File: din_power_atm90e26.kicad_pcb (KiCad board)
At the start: 2 copper layers, 86.9 x 32.8 mm, 62 parts, among them J1 CONN_01X06, J2 VBAT, J3 CONN_01X08, J4 CONN_02X18, J5 CONN_01X08, U1 MCP73831-2-OT, U2 AP7365-33YG-13, U3 AP7365-33YG-13, U4 Hi-Link_SMPS, U5 dc-dc

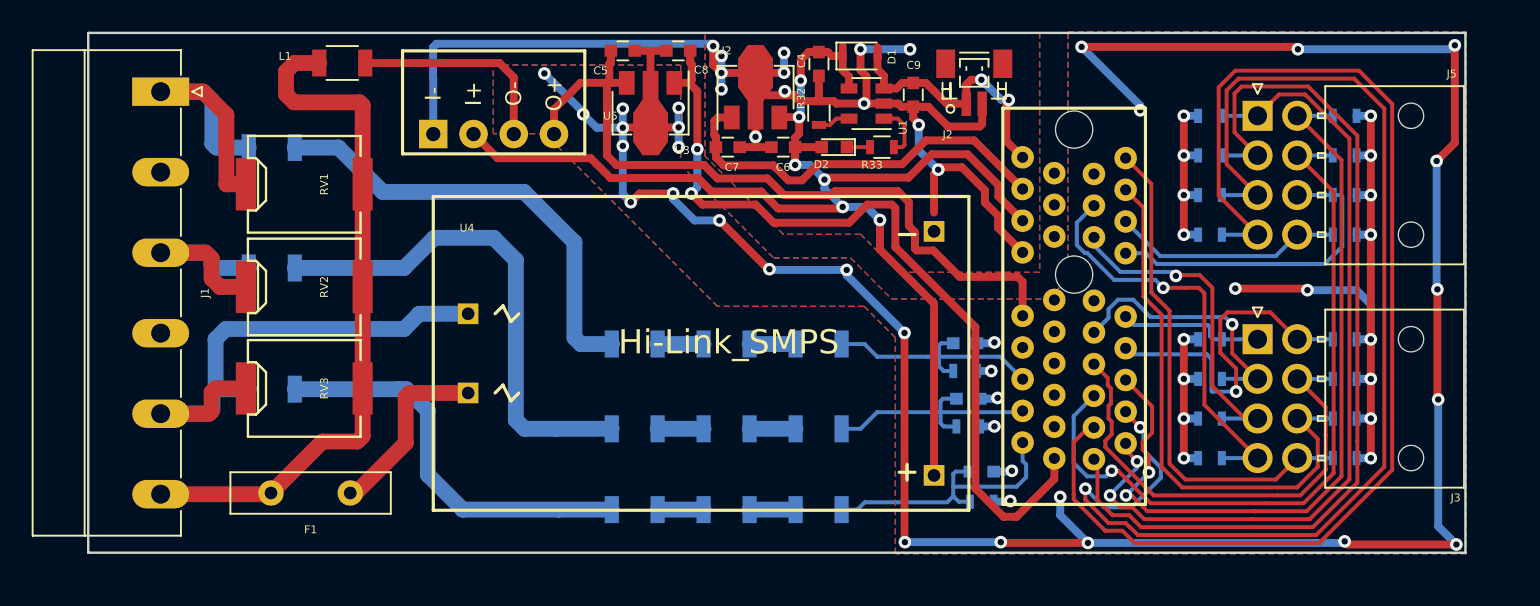
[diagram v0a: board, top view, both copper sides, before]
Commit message: First pass at layout matching meter PCB
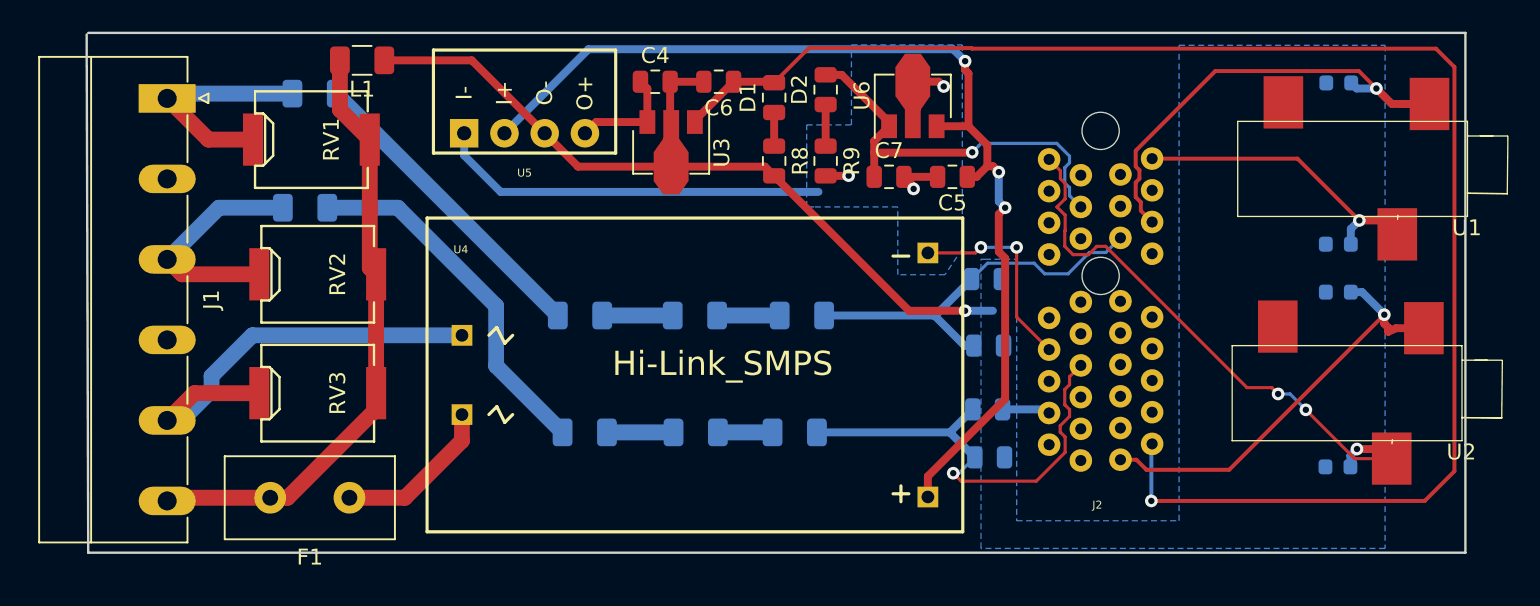
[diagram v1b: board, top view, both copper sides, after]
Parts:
- removed C2: 33n, Capacitors_SMD:C_0603
- removed C8, C9: 1uF, Capacitors_SMD:C_0603
- removed J3, J5: CONN_01X08, Connectors_Molex:Molex_NanoFit_2x04x2.50mm_Angled
- removed J4: CONN_02X18, hi-link_smps:PCIE-36-SKT
- removed LOGO_OSHW1: Logo_Open_Hardware_Small, Symbols:OSHW-Symbol_6.7x6mm_SilkScreen
- removed R10, R11, R18, R19, R20, R21, R28, R29, R30, R31: 5.8R, Resistors_SMD:R_0603
- removed R14, R17, R24, R7: 220K, Resistors_SMD:R_1206
- removed R27, R33: 1K, Resistors_SMD:R_0603
- removed R32: 2K, Resistors_SMD:R_0603
- added U6: AP7365-33YG-13, Package_TO_SOT_SMD:SOT-89-3, F.Cu at (157.9, 49.9)
- C1, C3: value 33n -> .033u; footprint Capacitors_SMD:C_0603 -> Capacitor_SMD:C_0805_2012Metric
- C4, C5, C6, C7: value 1uF -> 1u; footprint Capacitors_SMD:C_0603 -> Capacitor_SMD:C_0805_2012Metric
- D1: value D_Schottky -> IND_LED; footprint Diodes_SMD:D_SOD-323F -> Capacitor_SMD:C_0805_2012Metric
- D2: value LED -> IND_LED; footprint LEDs:LED_0603 -> Capacitor_SMD:C_0805_2012Metric
- F1: footprint Capacitors_THT:C_Disc_D10.0mm_W2.5mm_P5.00mm -> Capacitor_THT:C_Disc_D10.5mm_W5.0mm_P5.00mm
- J2: value VBAT -> CONN_02X18; footprint Connectors_JST:JST_SH_BM02B-SRSS-TB_02x1.00mm_Straight -> hi-link_smps:PCIE-36-SKT
- L1: footprint Inductors_SMD:L_1206 -> Inductor_SMD:L_1206_3216Metric
- R1, R2, R3, R4: footprint Resistors_SMD:R_0603 -> Resistor_SMD:R_0603_1608Metric
- R12, R13, R15, R16, R22, R23, R5, R6: footprint Resistors_SMD:R_1206 -> Resistor_SMD:R_1206_3216Metric
- R25, R26: footprint Resistors_SMD:R_0603 -> Resistor_SMD:R_0805_2012Metric
- R8, R9: value 5.8R -> 499; footprint Resistors_SMD:R_0603 -> Resistor_SMD:R_0805_2012Metric; moved to F.Cu
- U1: value MCP73831-2-OT -> TRS35_3; footprint TO_SOT_Packages_SMD:SOT-23-5 -> HappyDayEnergyMonitor:Audio-Jack
- U2: value AP7365-33YG-13 -> TRS35_3; footprint TO_SOT_Packages_SMD:SOT-89-3 -> HappyDayEnergyMonitor:Audio-Jack
- U3: footprint TO_SOT_Packages_SMD:SOT-89-3 -> Package_TO_SOT_SMD:SOT-89-3
- moved U2 49.7 mm to (192.6, 71.2), turned to 180 degrees
- moved U1 38.6 mm to (192.9, 57.0)
- moved R8 27.6 mm to (149.2, 53.5), turned to 270 degrees
- moved R9 24.7 mm to (152.4, 53.5), turned to 270 degrees
- moved C5 22.3 mm to (160.4, 54.5), turned to 180 degrees
- moved R4 19.7 mm to (184.8, 72.8), turned to 180 degrees
- moved SYM1 16.0 mm to (132.3, 57.9)
- moved J2 14.5 mm to (169.8, 60.8), turned to 90 degrees
- moved R3 11.1 mm to (184.8, 61.8), turned to 0 degrees
- moved C4 10.4 mm to (141.7, 48.5), turned to 0 degrees
- moved C7 10.3 mm to (156.4, 54.5)
- moved R2 9.85 mm to (184.8, 58.8)
- moved R1 8.39 mm to (184.8, 48.6)
- moved D1 6.03 mm to (149.2, 49.5), turned to 90 degrees
- moved C6 5.80 mm to (145.7, 48.5)
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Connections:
- C1 pad 1: UB_SAMP -> VP_1
- C1 pad 2: GNDA -> GND_M
- C3 pad 1: UA_SAMP -> VP_0
- C3 pad 2: GNDA -> GND_M
- C4 pad 1: +5V -> +5V_ISO
- C4 pad 2: GNDPWR -> GND_M
- C5 pad 1: +5V_ISO -> +5V
- C5 pad 2: GNDA -> GND_CPU
- C6 pad 1: +5V -> 3V3_M
- C6 pad 2: GNDPWR -> GND_M
- C7 pad 1: +3V3 -> 3V3_CPU
- C7 pad 2: GNDPWR -> GND_CPU
- D1 pad 1: +5V -> Net-(D1-Pad1)
- D1 pad 2: VBAT -> 3V3_M
- D2 pad 2: +5V -> 3V3_CPU
- J2 pad 1: VBAT -> 3V3_M
- J2 pad 2: GNDPWR -> VP_1
- L1 pad 1: GNDA -> GND_M
- R1 pad 1: GNDA -> GND_M
- R1 pad 2: IA1+ -> I1P_0_IN
- R2 pad 1: IA1- -> I1N_0_N
- R2 pad 2: GNDA -> GND_M
- R22 pad 1: UA_SAMP -> VP_0
- R23 pad 1: UB_SAMP -> VP_1
- R25 pad 1: GNDA -> GND_M
- R25 pad 2: UA_SAMP -> VP_0
- R26 pad 1: GNDA -> GND_M
- R26 pad 2: UB_SAMP -> VP_1
- R3 pad 1: GNDA -> GND_M
- R3 pad 2: IC1+ -> I1P_1_IN
- R4 pad 1: IC1- -> I1N_1_IN
- R4 pad 2: GNDA -> GND_M
- R8 pad 1: GNDA -> Net-(D1-Pad1)
- R8 pad 2: IB1+ -> GND_M
- R9 pad 1: IB1- -> Net-(D2-Pad1)
- R9 pad 2: GNDA -> GND_CPU
- U1 pad 1: Net-(R33-Pad2) -> I1N_0_N
- U1 pad 2: GNDPWR -> I1P_0_IN
- U1 pad 3: VBAT -> Net-(U1-Pad3)
- U2 pad 1: +3V3 -> I1N_1_IN
- U2 pad 2: GNDPWR -> I1P_1_IN
- U2 pad 3: +5V -> Net-(U2-Pad3)
- U3 pad 1: +3.3V_ISO -> 3V3_M
- U3 pad 2: GNDA -> GND_M
- U4 pad 3: GNDPWR -> GND_CPU
- U5 pad 1: GNDPWR -> GND_CPU
- U5 pad 3: GNDA -> GND_M
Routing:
- net GNDA: track 239.7 -> 0.00 mm, vias 51 -> 0
- net 3V3_M: track 0.00 -> 99.5 mm, vias 0 -> 1
- net GNDPWR: track 78.1 -> 0.00 mm, vias 13 -> 0
- net IB1+: track 76.9 -> 0.00 mm, vias 2 -> 0
- net IB1-: track 76.8 -> 0.00 mm
- net IA1-: track 59.7 -> 0.00 mm
- net GND_M: track 0.00 -> 57.6 mm, vias 0 -> 1
- net IA1+: track 52.5 -> 0.00 mm, vias 2 -> 0
- net +3.3V_ISO: track 52.5 -> 0.00 mm, vias 2 -> 0
- net IC1+: track 50.2 -> 0.00 mm, vias 2 -> 0
- net GND_CPU: track 0.00 -> 48.8 mm, vias 0 -> 5
- net IC1-: track 46.9 -> 0.00 mm, vias 1 -> 0
- net +5V_ISO: track 47.1 -> 6.96 mm
- net I1N_1_IN: track 0.00 -> 36.7 mm, vias 0 -> 3
- net IN2+: track 35.2 -> 0.00 mm
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- added copper zone on B.Cu, net GND_CPU
- added copper zone on B.Cu, net GND_M
- removed copper zone on B.Cu, net GNDA
- removed copper zone on F.Cu, net GNDA
- removed copper zone on B.Cu, net GNDPWR
- removed copper zone on F.Cu, net GNDPWR
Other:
- board size 86.9 x 32.8 mm -> 87 x 32.8 mm
- board text added: "Thanks to"
- board text removed: "TAPR"
- board text removed: "Whatnick Emon Base v1.2 07/12/2017"
